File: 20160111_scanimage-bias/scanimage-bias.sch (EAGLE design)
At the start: 4 parts

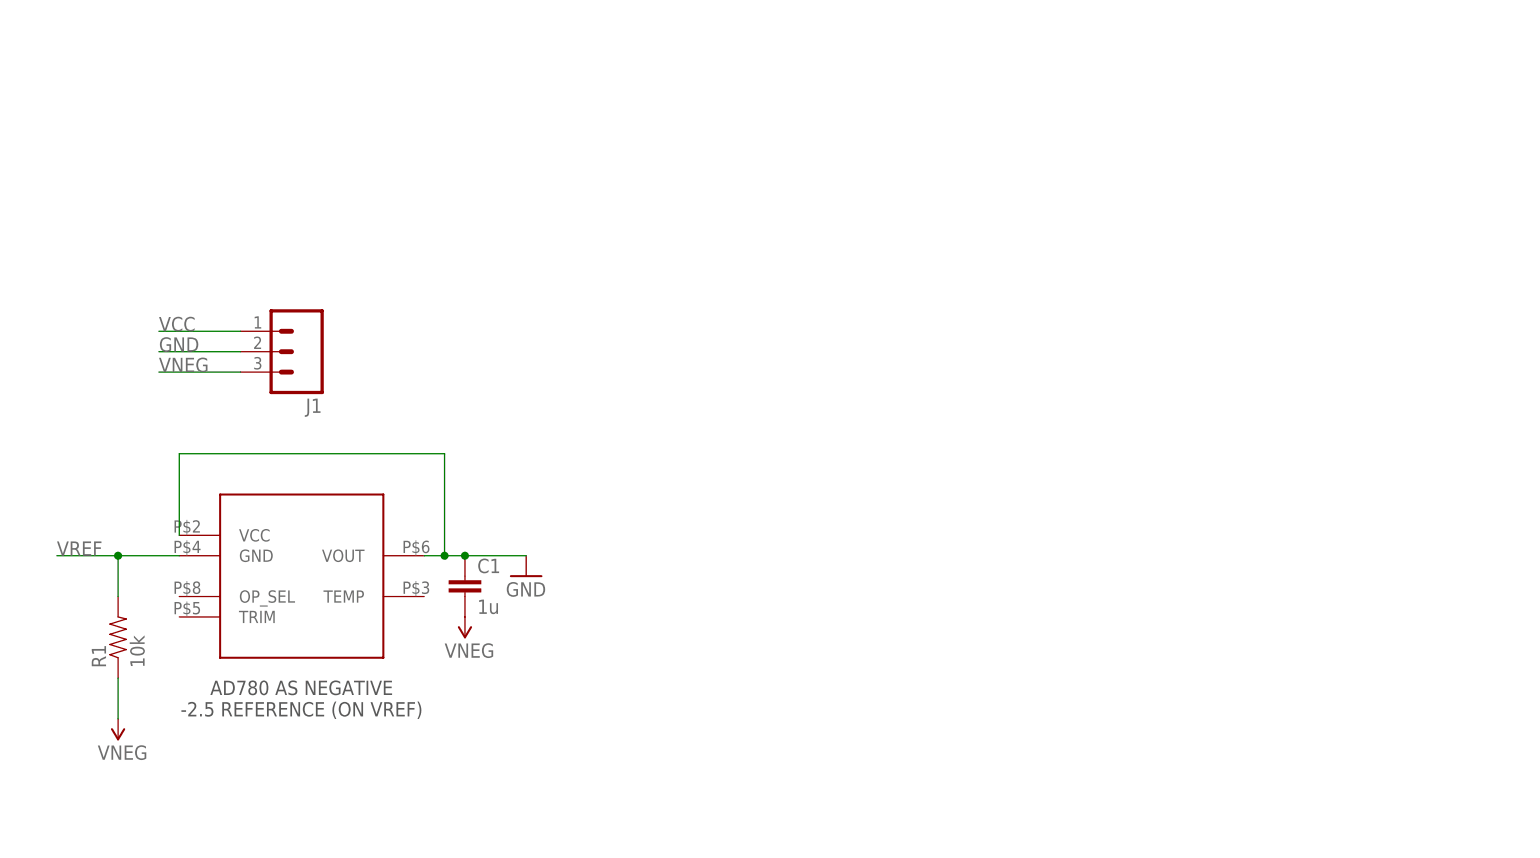
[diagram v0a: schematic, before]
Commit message: Finish schematic
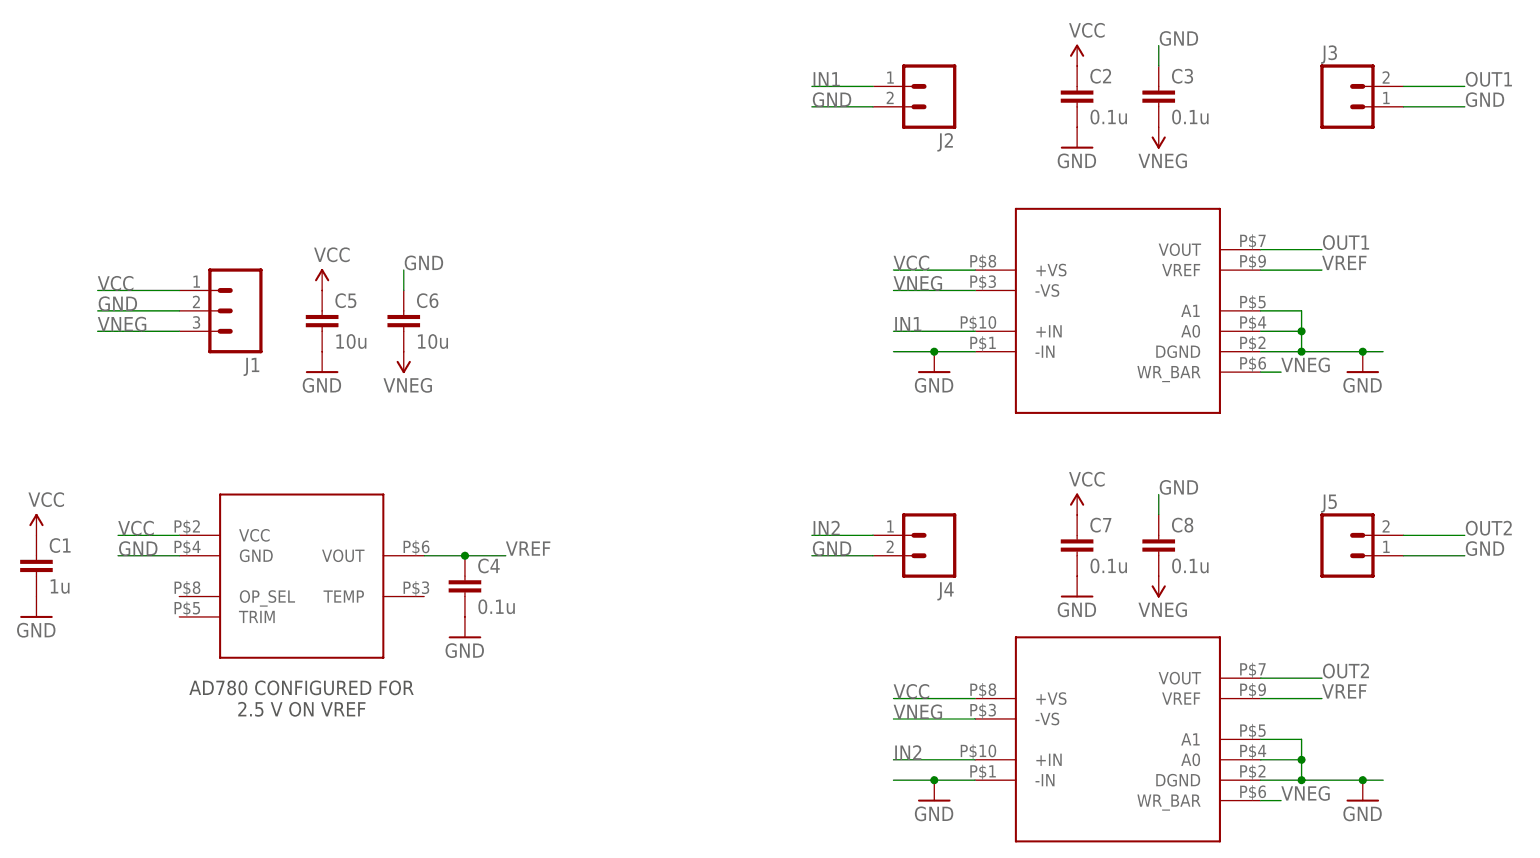
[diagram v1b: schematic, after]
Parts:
- removed R1: 10k, SparkFun-Resistors:RESISTOR1206
- added C2, C3, C4, C7, C8: 0.1u, SparkFun-Capacitors:CAP1206
- added C5, C6: 10u, SparkFun-Capacitors:CAP1206
- added J2, J3, J4, J5: (no value), SparkFun-Connectors:M02PTH
- added U$2, U$3: AD8250, kimth:AD8250
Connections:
- new net IN1: J2.1, U$2.+IN
- new net IN2: J4.1, U$3.+IN
- new net OUT1: J3.2, U$2.VOUT
- new net OUT2: J5.2, U$3.VOUT
- net GND: now also C1.2, C2.2, C3.1, C4.2, C5.2, C6.1, C7.2, C8.1, J2.2, J3.1, J4.2, J5.1, U$1.GND, U$2.-IN, U$2.A0, U$2.A1, U$2.DGND, U$3.-IN, U$3.A0, U$3.A1, U$3.DGND; no longer C1.1, U$1.VCC, U$1.VOUT
- net VCC: now also C1.1, C2.1, C5.1, C7.1, U$1.VCC, U$2.+VS, U$3.+VS
- net VNEG: now also C3.2, C6.2, C8.2, U$2.-VS, U$2.WR_BAR, U$3.-VS, U$3.WR_BAR; no longer C1.2, R1.1
- net VREF: now also C4.1, U$1.VOUT, U$2.VREF, U$3.VREF; no longer R1.2, U$1.GND
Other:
- note added: "AD780 CONFIGURED FOR 2.5 V ON VREF"
- note removed: "AD780 AS NEGATIVE -2.5 REFERENCE (ON VREF)"
- moved on the sheet: C1, J1
